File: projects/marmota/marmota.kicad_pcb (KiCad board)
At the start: 2 copper layers, 70 x 70 mm, 64 parts, among them J1 USB_C, J2 Conn_01x20_Pin, J3 Conn_01x20_Pin, SW1 Button top, SW2 Button side, U1 RP2040, U2 FLASH, U3 MCP73871, U4 RT6150B, U5 ESP32, Y1 12MHz

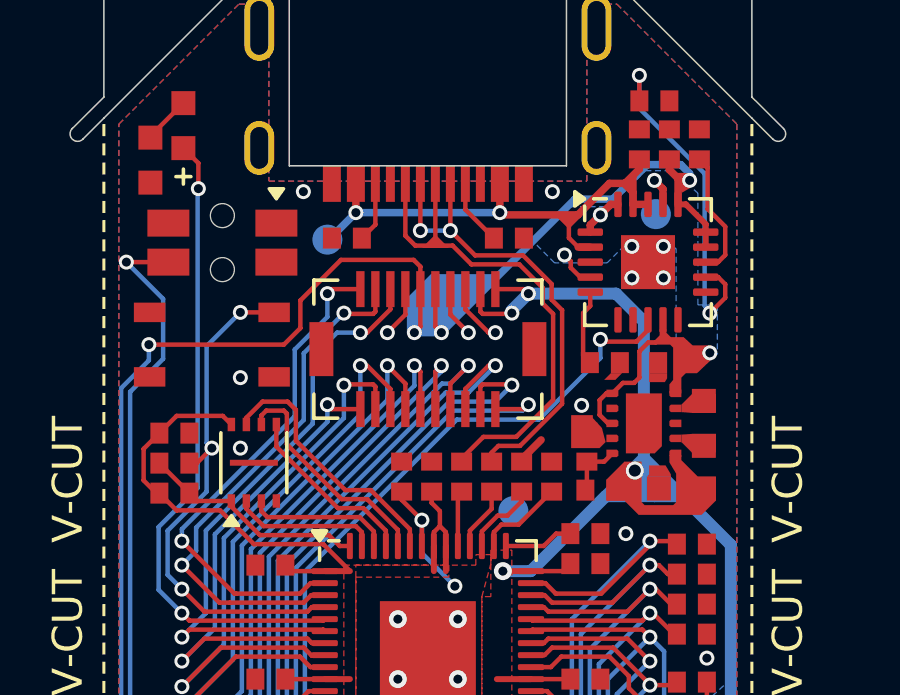
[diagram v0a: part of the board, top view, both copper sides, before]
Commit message: Richtek power saving high, Tweaks
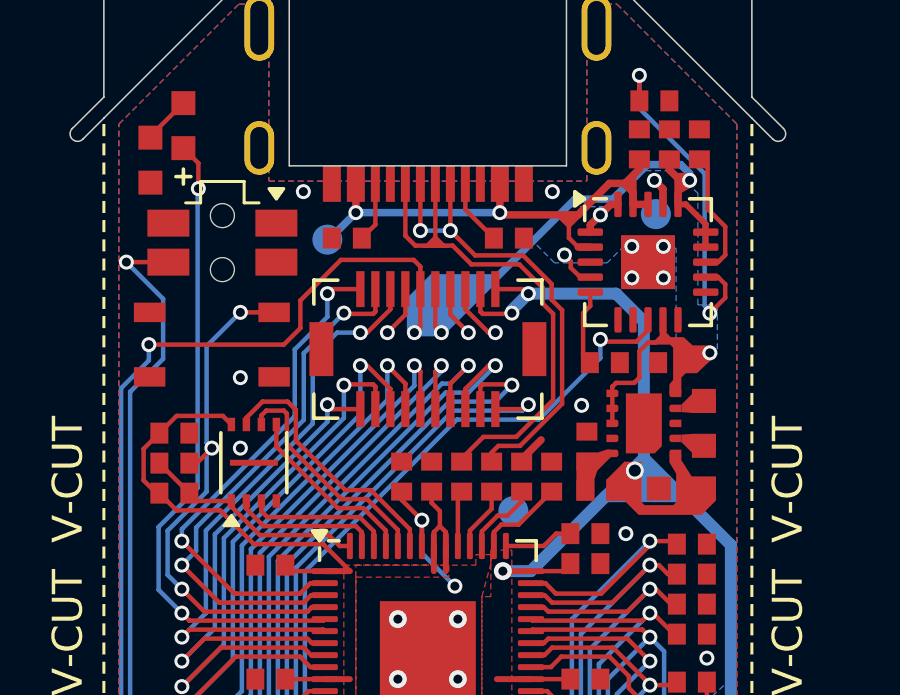
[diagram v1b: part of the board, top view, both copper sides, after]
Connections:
- U4 pad 7: GND -> VSYS
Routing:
- net Net-(U4-FB): track 1.93 -> 0.00 mm

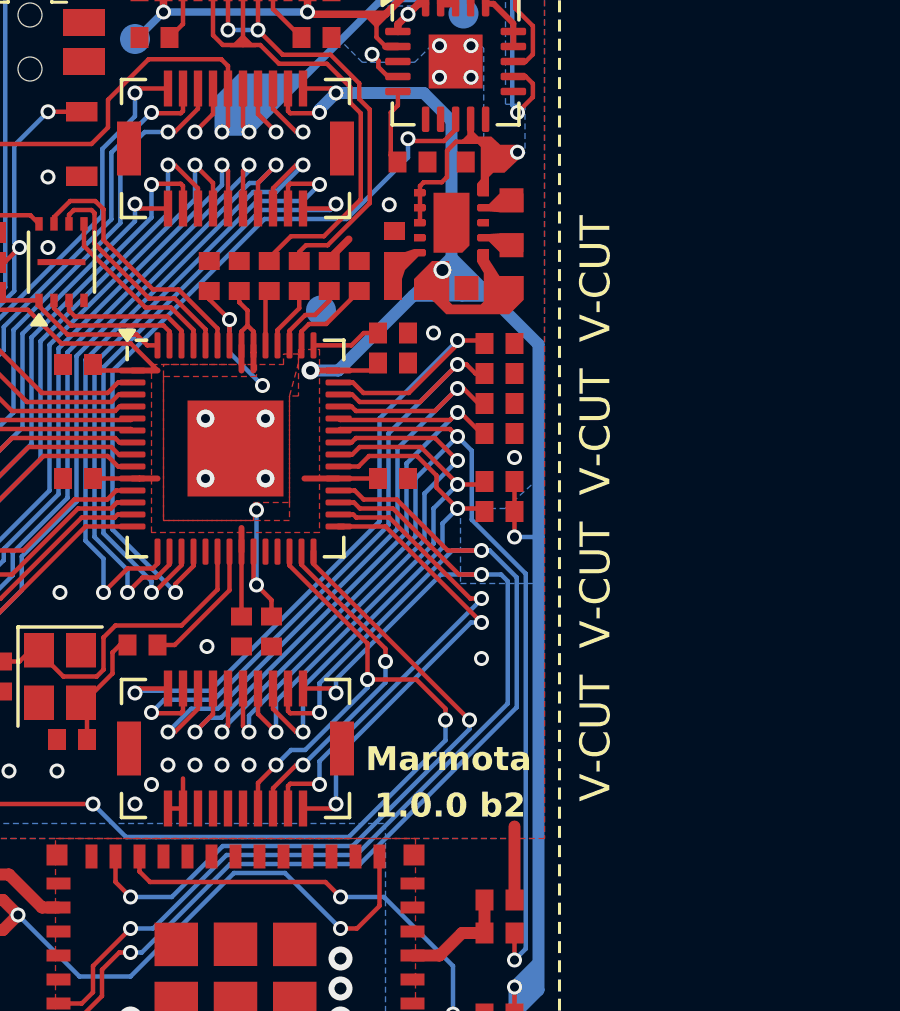
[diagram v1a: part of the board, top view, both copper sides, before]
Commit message: Marmota RT6150 power save mode enabled, Replacement for crystal oscillator
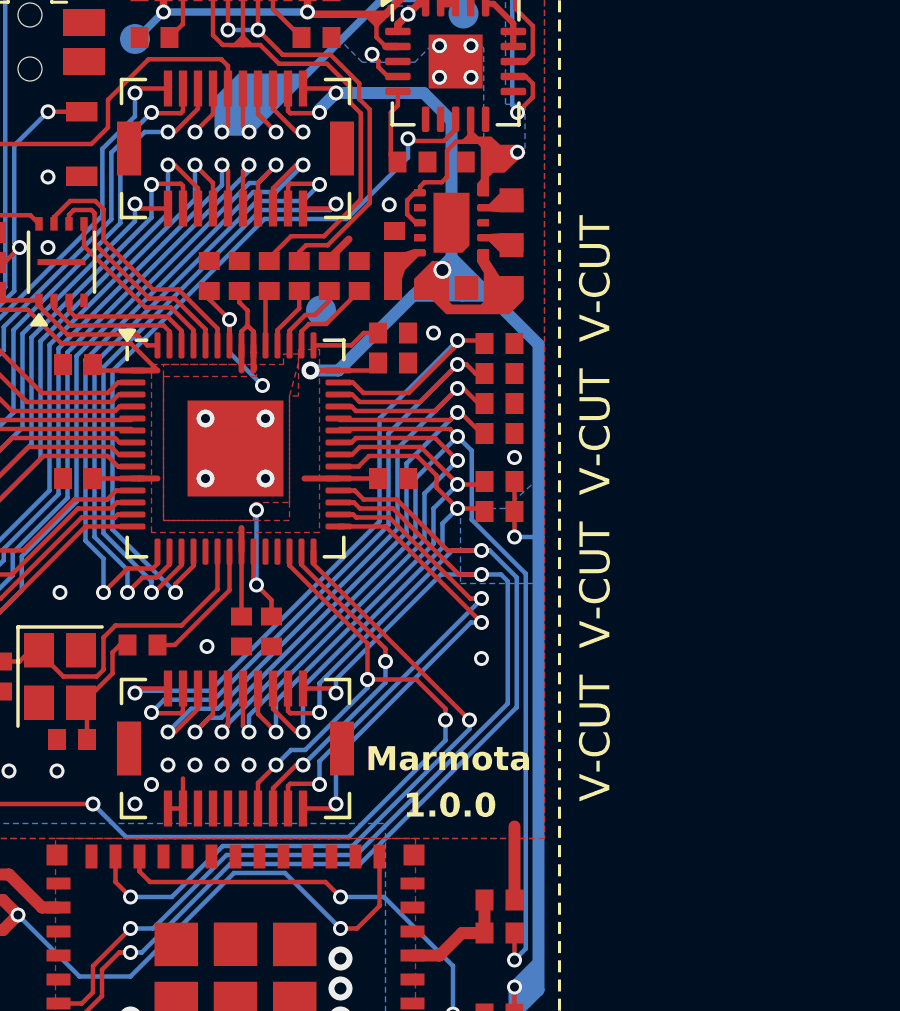
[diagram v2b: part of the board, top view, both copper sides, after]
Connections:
- U4 pad 7: VSYS -> GND
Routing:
- net VSYS: track 8.30 -> 8.83 mm
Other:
- board text added: "1.0.0"
- board text added: "Input Labs Oy. Marmota 1.0.0"
- board text removed: "1.0.0 b2"
- board text removed: "Input Labs Oy. Marmota 1.0.0 beta2"
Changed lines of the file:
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@@
 			(chamfer_ratio 0.2)
 			(chamfer top_right bottom_right)
-			(net 55 "VSYS")
+			(net 1 "GND")
 			(pinfunction "PS")
 			(pintype "input")
@@
 			)
 		)
-		(property "LCSC" "C2149205"
+		(property "LCSC" "C2896601"
 			(at 0 0 -90)
 			(unlocked yes)
@@
 		(layer "Edge.Cuts")
 	)
-	(gr_text "Input Labs Oy.\nMarmota\n1.0.0 beta2"
+	(gr_text "Input Labs Oy.\nMarmota\n1.0.0"
 		(at 66.65 62.75 270)
 		(layer "B.SilkS")
@@
 		)
 	)
-	(gr_text "1.0.0 b2"
+	(gr_text "1.0.0"
 		(at 67.15 63.9 0)
 		(layer "F.SilkS")
@@
 	)
 	(segment
+		(start 67.8375 41.025)
+		(end 67.8375 41.5375)
+		(width 0.15)
+		(layer "F.Cu")
+		(net 55)
+	)
+	(segment
 		(start 67.8375 41.5375)
 		(end 67.6 41.775)
@@
 	)
 	(segment
-		(start 67.8375 41.025)
-		(end 67.8375 41.5375)
+		(start 66.15 43.275)
+		(end 66.15 43.475)
+		(width 0.15)
+		(layer "F.Cu")
+		(net 55)
+	)
+	(segment
+		(start 65.725 43.725)
+		(end 65.975 43.475)
 		(width 0.15)
 		(layer "F.Cu")
@@
 	)
 	(segment
-		(start 66.875 43.125)
-		(end 66.275 43.125)
+		(start 66.15 44.475)
+		(end 66.006801 44.475)
+		(width 0.15)
+		(layer "F.Cu")
+		(net 55)
+	)
+	(segment
+		(start 65.4125 37.8625)
+		(end 65.4125 38.1)
+		(width 0.25)
+		(layer "F.Cu")
+		(net 55)
+	)
+	(segment
+		(start 67.6 41.775)
+		(end 67.35 41.775)
 		(width 0.15)
 		(layer "F.Cu")
@@
 	)
 	(segment
+		(start 66.006801 44.475)
+		(end 65.725 44.193199)
+		(width 0.15)
+		(layer "F.Cu")
+		(net 55)
+	)
+	(segment
+		(start 66.1 37.175)
+		(end 66.3375 37.175)
+		(width 0.25)
+		(layer "F.Cu")
+		(net 55)
+	)
+	(segment
 		(start 67.05 42.95)
 		(end 66.875 43.125)
@@
 	)
 	(segment
-		(start 65.4125 37.8625)
-		(end 65.4125 38.1)
-		(width 0.25)
+		(start 67.35 41.775)
+		(end 67.05 42.075)
+		(width 0.15)
 		(layer "F.Cu")
 		(net 55)
 	)
 	(segment
-		(start 66.275 43.125)
-		(end 66.15 43.25)
+		(start 65.975 43.475)
+		(end 66.15 43.475)
 		(width 0.15)
 		(layer "F.Cu")
@@
 	)
 	(segment
-		(start 66.1 37.175)
-		(end 66.3375 37.175)
-		(width 0.25)
+		(start 66.3 43.125)
+		(end 66.15 43.275)
+		(width 0.15)
 		(layer "F.Cu")
 		(net 55)
@@
 	)
 	(segment
-		(start 65.07918 39.6)
-		(end 65.4125 39.6)
-		(width 0.15)
-		(layer "F.Cu")
-		(net 55)
-	)
-	(segment
-		(start 67.6 41.775)
-		(end 67.35 41.775)
+		(start 65.725 44.193199)
+		(end 65.725 43.725)
 		(width 0.15)
 		(layer "F.Cu")
@@
 	)
 	(segment
-		(start 67.35 41.775)
-		(end 67.05 42.075)
+		(start 65.07918 39.6)
+		(end 65.4125 39.6)
 		(width 0.15)
 		(layer "F.Cu")
@@
 	)
 	(segment
-		(start 66.15 43.25)
-		(end 66.15 44.475)
+		(start 66.875 43.125)
+		(end 66.3 43.125)
 		(width 0.15)
 		(layer "F.Cu")

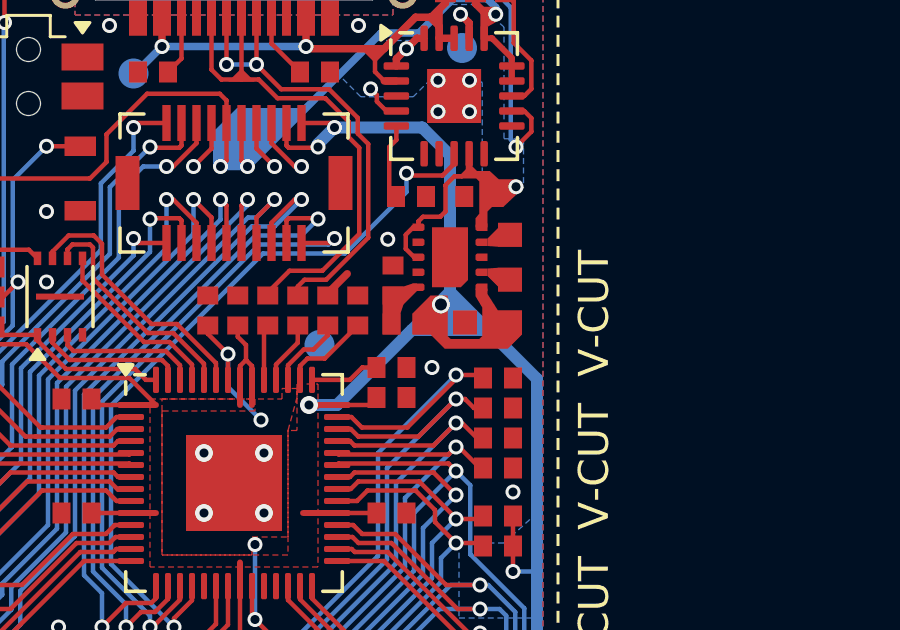
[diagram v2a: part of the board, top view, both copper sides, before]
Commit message: Marmota added 3V3 test point
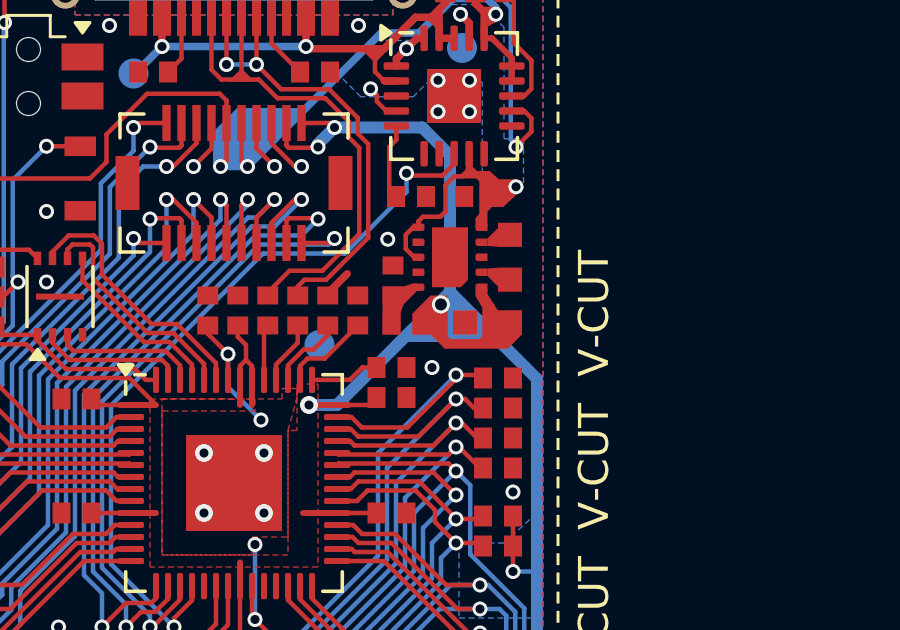
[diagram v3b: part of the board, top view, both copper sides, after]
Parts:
- added REF**: Pad_1mm, ILO_fp:Pad_1mm, B.Cu at (67.6, 46.7)
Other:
- board text added: "3V3"
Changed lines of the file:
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@@
+	(footprint "ILO_fp:Pad_1mm"
+		(layer "B.Cu")
+		(at 67.625 46.675 180)
+		(property "Reference" "REF**"
+			(at 1 0 0)
+			(unlocked yes)
+			(layer "B.SilkS")
+			(hide yes)
+			(effects
+				(font
+					(size 0.8 0.8)
+					(thickness 0.153)
+				)
+				(justify left mirror)
+			)
+		)
+		(property "Value" "Pad_1mm"
+			(at 0 3.8 180)
+			(layer "B.Fab")
+			(hide yes)
+			(effects
+				(font
+					(size 1 1)
+					(thickness 0.15)
+				)
+				(justify mirror)
+			)
+		)
+		(property "Footprint" "ILO_fp:Pad_1mm"
+			(at 0 0 0)
+			(unlocked yes)
+			(layer "B.Fab")
+			(hide yes)
+			(effects
+				(font
+					(size 1.27 1.27)
+					(thickness 0.15)
+				)
+				(justify mirror)
+			)
+		)
+		(property "Datasheet" ""
+			(at 0 0 0)
+			(unlocked yes)
+			(layer "B.Fab")
+			(hide yes)
+			(effects
+				(font
+					(size 1.27 1.27)
+					(thickness 0.15)
+				)
+				(justify mirror)
+			)
+		)
+		(property "Description" ""
+			(at 0 0 0)
+			(unlocked yes)
+			(layer "B.Fab")
+			(hide yes)
+			(effects
+				(font
+					(size 1.27 1.27)
+					(thickness 0.15)
+				)
+				(justify mirror)
+			)
+		)
+		(zone_connect 2)
+		(pad "1" smd circle
+			(at 0 0 180)
+			(size 1 1)
+			(layers "B.Cu" "B.Mask")
+			(net 7 "+3V3")
+		)
+	)
 	(footprint "ILO_fp:Pad_1mm"
 		(layer "B.Cu")
@@
 	(gr_poly
 		(pts
-			(xy 68.95 47.1) (xy 67.35 45.5) (xy 67.05 45.5) (xy 65.45 47.1)
+			(xy 69.15 47.3) (xy 67.35 45.5) (xy 67.05 45.5) (xy 65.25 47.3)
 		)
 		(stroke
@@
 		)
 	)
+	(gr_text "3V3"
+		(at 66.018927 46.149868 270)
+		(layer "B.SilkS")
+		(effects
+			(font
+				(size 0.8 0.8)
+				(thickness 0.15)
+				(bold yes)
+			)
+			(justify mirror)
+		)
+	)

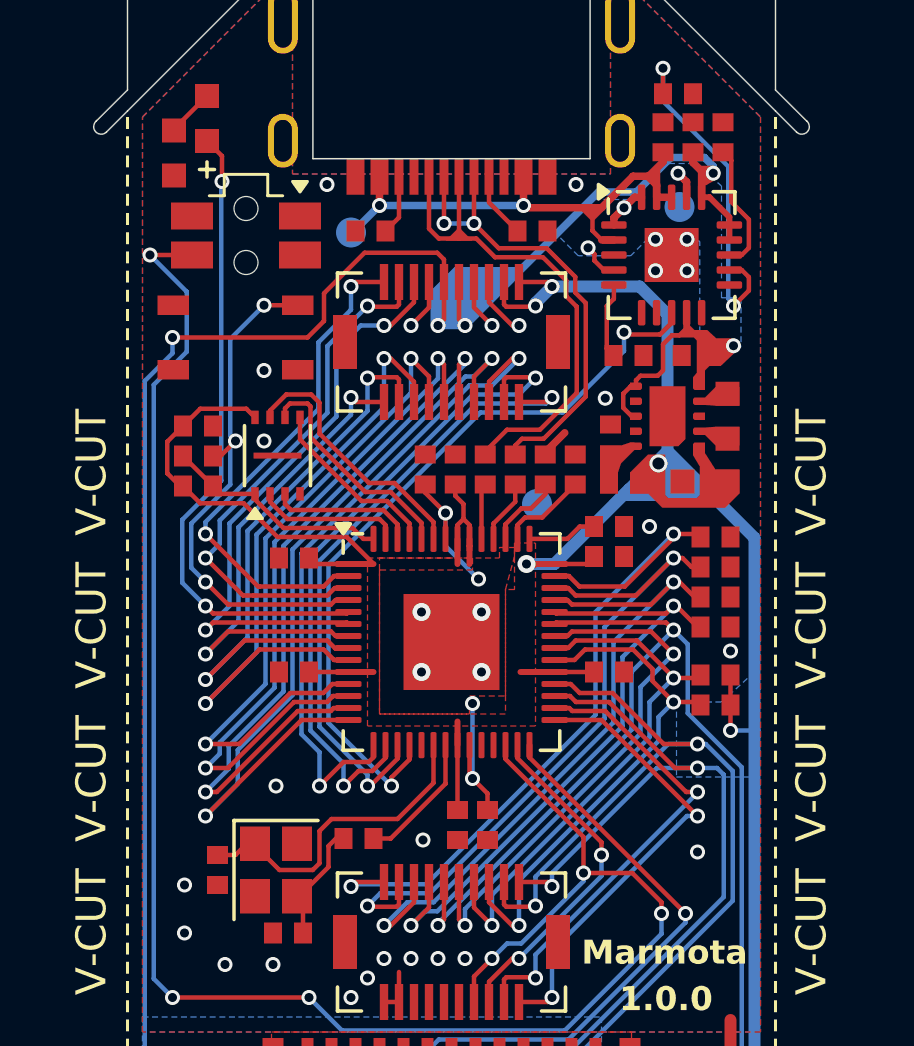
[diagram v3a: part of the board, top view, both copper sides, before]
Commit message: Connected RT buckboost power save pin to gpio, Shifted GPIOs
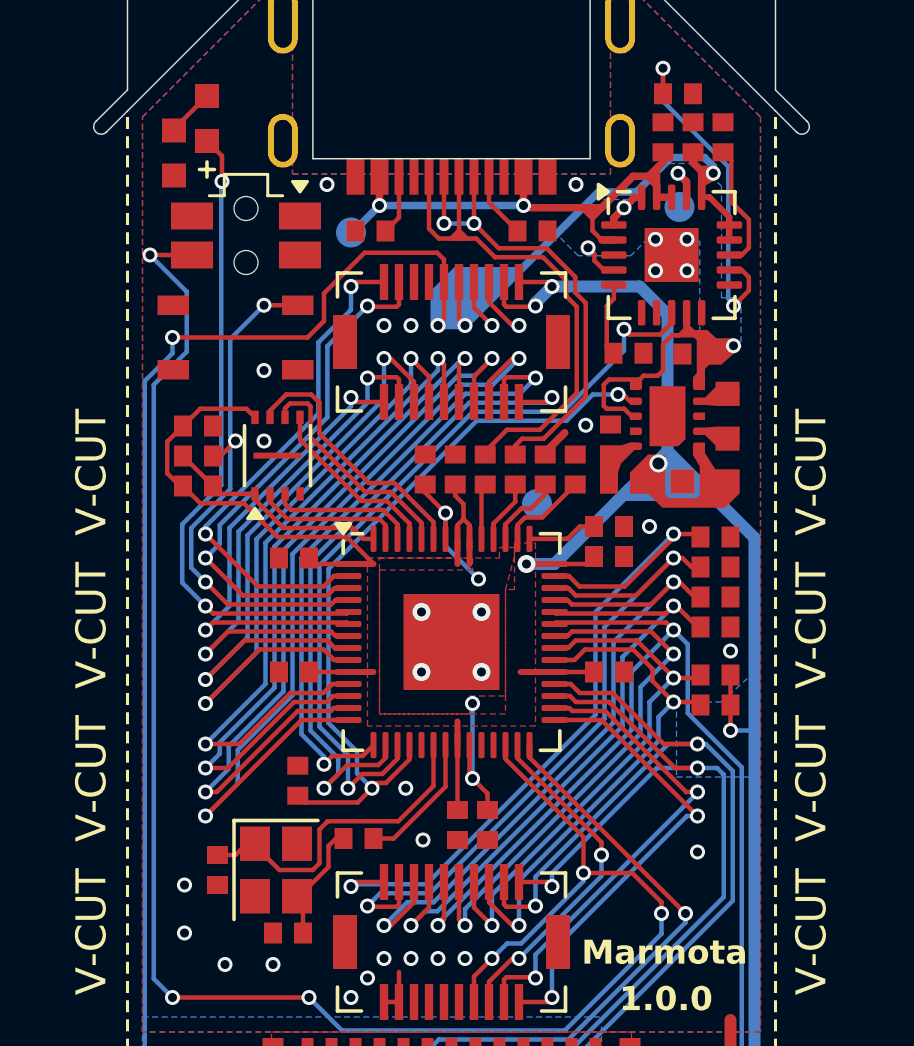
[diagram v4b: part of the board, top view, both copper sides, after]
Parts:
- added R37: 86.6KΩ, ILO_fp:0402_compact, F.Cu at (54.9, 56.6)
- moved R34 0.08 mm to (65.9, 42.4)
- moved C41 0.06 mm to (68.2, 42.4)
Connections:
- J2 pad 11: /GP5 -> /GP4
- J2 pad 12: /GP6 -> /GP5
- J2 pad 13: /GP7 -> /GP6
- J2 pad 14: /GP8 -> /GP7
- J2 pad 15: /GP9 -> /GP8
- J2 pad 16: /GP10 -> /GP9
- J2 pad 17: /GP11 -> /GP10
- J2 pad 18: /GP12 -> /GP11
- J2 pad 19: /GP13 -> /GP12
- J2 pad 20: /GP14 -> /GP13
- J2 pad 3: /GP4 -> unconnected-(J2-Pin_3-Pad3)
- J2 pad 4: GND -> unconnected-(J2-Pin_4-Pad4)
- U3 pad 8: /GP15 -> /GP14
- U4 pad 7: GND -> /GP15
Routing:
- net /GP14: track 21.2 -> 26.3 mm
- net /GP4: track 20.0 -> 15.8 mm
- net GND: track 16.2 -> 14.5 mm, vias 37 -> 38
- net /GP5: track 16.9 -> 18.4 mm
- net VSYS: track 8.83 -> 10.1 mm
- net /GP12: track 22.5 -> 21.2 mm
- net /GP11: track 27.2 -> 28.3 mm
- net /GP6: track 19.5 -> 20.6 mm
- net /GP10: track 25.6 -> 26.4 mm
